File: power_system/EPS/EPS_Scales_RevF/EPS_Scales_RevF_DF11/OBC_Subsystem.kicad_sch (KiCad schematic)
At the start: 50 parts, among them J10 DF11-16DP-2DSA, U17 TPS1HB08BQPWPRQ1, U3 LT8612EUDE#PBF, U5 INA260AIPWR, U7 LTC6902, U9 TCA4307DGKR

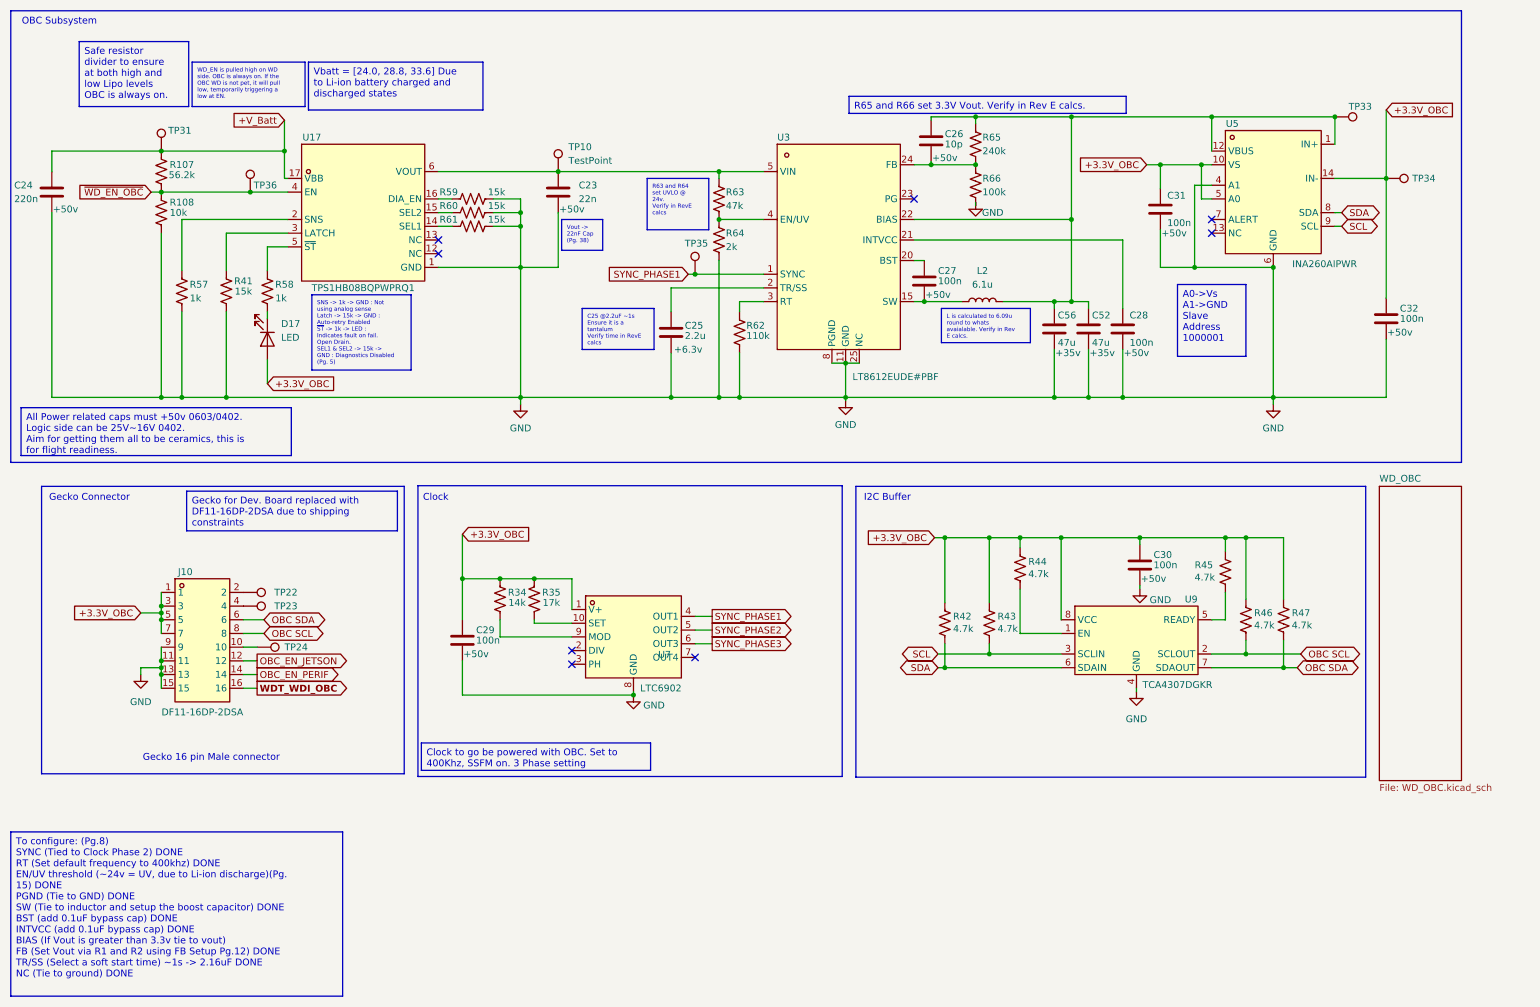
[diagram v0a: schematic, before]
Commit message: Completed EPS REV F / Viking 1-C PCB
Fixed minor issue with the extra resistor for the EN line VD, and added temperature sensors for each subsystem.
Also, the JPL logo is back!
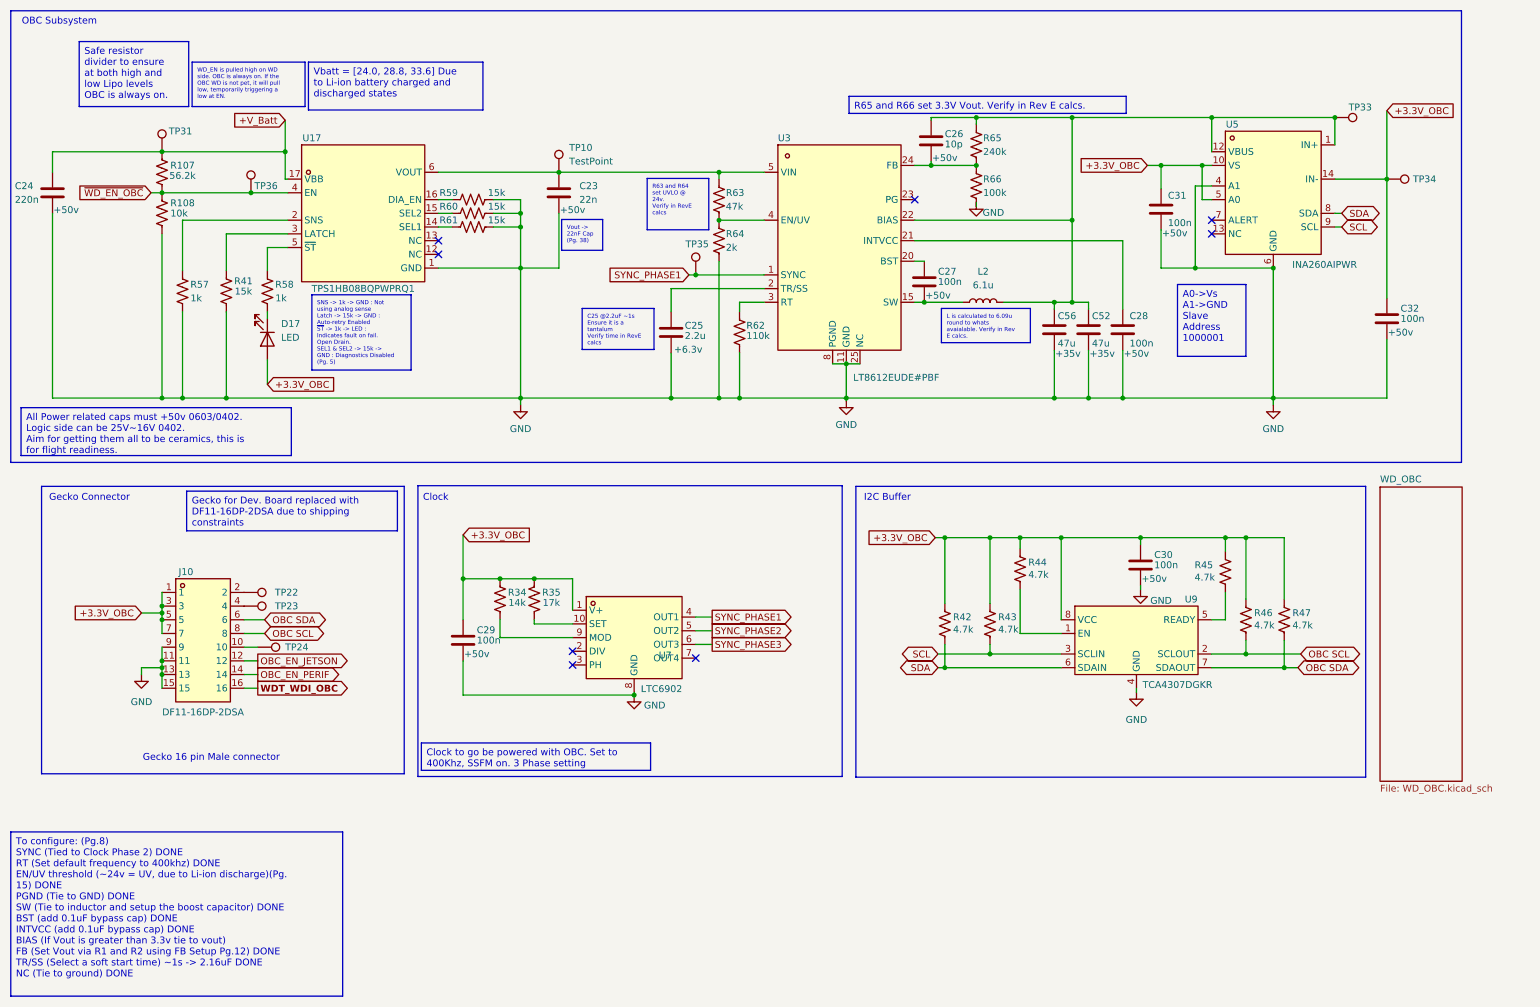
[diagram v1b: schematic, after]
